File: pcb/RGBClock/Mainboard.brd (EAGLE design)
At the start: 100 x 80 mm, 88 parts, among them IC1 MCP23017SO, K1 G6K-2F, K2 G6K-2F, K3 G6K-2F, K4 G6K-2F, U1 71918-126LF, U10 2N7002-7-F, U11 2N7002-7-F, U12 2N7002-7-F, U13 NX3L1G384GW, U14 NX3L1G384GW, U15 NX3L1G384GW, U16 NX3L1G384GW, U2 LM2675M-5.0, U3 TXS0102DCUR, U4 P82B96DR, U5 TPS71533DCKR, U6 DS1338Z-33+, U7 MAX6369KA+T, U8 DRV612PW, U9 2N7002-7-F, X12 1503_09, X13 1503_09, X2 5566-4, X3 5566-8

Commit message: Mainboard + displayboard
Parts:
- removed U$1: SRR1240-680M, Bourns_By_element14_Batch_1:SRR1240
- removed U$2: 68u, MyComponents:594D-B
- removed U$3: SI4735-D50, SiliconLabs:SSOP24
- removed U$4, U$7: CDSOD323-T03C, MyComponents:SOD323
- removed U$5, U$6: SMA6F, MyComponents:DO-221AC
- removed X12: 1503_09, con-lumberg:1503_09
- added C18: 1u, rcl:C1005
- added D10: 1N4148DO35-7, diode:DO35-7
- added D3: SMA6F, MyComponents:DO-221AC
- added D5, D6: CDSOD323-T03C, MyComponents:SOD323
- added L1: SRR1240-680M, Bourns_By_element14_Batch_1:SRR1240
- added U17: 2N7002-7-F, Diodes:SOT103P240X110-3N
- added X5: 5566-8, con-molex:5566-8
- C10: value 1u -> 22p
- C11: value 1u -> 100n
- C12: value 1u -> 22n
- C13: value 22p -> 0,47u; device rcl:C1005 -> rcl:C1206
- C14: value 22p -> 2u2
- C15: value 1n -> 2u2
- C16: value 22n -> 1u
- C17: value 100n -> 1u
- C4: value 100n -> 594D686X0010C2T; device rcl:C0805 -> MyComponents:594D-B
- C5: value 0,47u -> 1n; device rcl:C1206 -> rcl:C1005
- C6: value 2u2 -> 22p
- C7: value 2u2 -> 100n; device rcl:C1005 -> rcl:C0805
- D2: value 1N4148DO35-7 -> SMA6F; device diode:DO35-7 -> MyComponents:DO-221AC
- R10, R11, R8, R9: value (none) -> 47K; device resistor:R2012 -> resistor:0204V
- R13: value 680R -> 4K7
- R14: value 680R -> A2-1; device resistor:0204V -> resistor:R0402
- R15: value 100R -> A2-0; device resistor:0204V -> resistor:R0402
- R16: value 47K -> A1-1; device resistor:0204V -> resistor:R0402
- R17: value 47K -> A1-0; device resistor:0204V -> resistor:R0402
- R18: value 47K -> A0-1; device resistor:0204V -> resistor:R0402
- R19: value 47K -> A0-0; device resistor:0204V -> resistor:R0402
- R4: value 4K7 -> 680R
- R5: value 100R -> 680R
- R6, R7: value (none) -> 100R; device resistor:R2012 -> resistor:0204V
- U10, U11, U12, U9: value 2N7002-7-F -> NX3L1G384GW; device Diodes:SOT103P240X110-3N -> NXP_By_element14_Batch_1:SOT65P212X110-5N
- U13: value NX3L1G384GW -> DRV612PW; device NXP_By_element14_Batch_1:SOT65P212X110-5N -> Texas:SOP65P640X120-14N
- U14, U15, U16: value NX3L1G384GW -> 2N7002-7-F; device NXP_By_element14_Batch_1:SOT65P212X110-5N -> Diodes:SOT103P240X110-3N
- U2: value LM2675M-5.0 -> MAX6369KA+T; device Texas:SOIC127P620X175-8N -> Maxim_By_element14_Batch_1:SOT65P280X145-8N
- U5: value TPS71533DCKR -> LM2675M-5.0; device Texas:SOT65P210X110-5N -> Texas:SOIC127P620X175-8N
- U7: value MAX6369KA+T -> SI4735-D50; device Maxim_By_element14_Batch_1:SOT65P280X145-8N -> SiliconLabs:SSOP24
- U8: value DRV612PW -> TPS71533DCKR; device Texas:SOP65P640X120-14N -> Texas:SOT65P210X110-5N
- X3: value 5566-8 -> 1503_09; device con-molex:5566-8 -> con-lumberg:1503_09
- moved X3 103.4 mm to (1.27, 59.7)
- moved R13 62.3 mm to (76.2, 38.1)
- moved R4 62.3 mm to (15.2, 50.8)
- moved C5 47.4 mm to (45.7, 29.2)
- moved C12 44.6 mm to (39.4, 31.8), turned to 0 degrees
- moved C16 44.4 mm to (82.5, 41.9)
- moved R14 44.3 mm to (40.9, 17.8), turned to 0 degrees
- moved R9 40.9 mm to (63.5, 48.3)
- moved U5 40.9 mm to (31.8, 62.2)
- moved C13 40.3 mm to (62.2, 73.7)
- moved D2 40.2 mm to (26.2, 37.8)
- moved C10 40.1 mm to (43.2, 34.3)
- moved R17 39.0 mm to (37.6, 19.1)
- moved R10 38.1 mm to (57.1, 48.3)
- moved R15 35.7 mm to (37.6, 17.8), turned to 0 degrees
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- renumbered Q3 to Q1, Q4 to Q2, X13 to X4, X7 to X1
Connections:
- net +3V3: now also C11.1, C12.1, C13.1, C17.2, R10.1, R14.2, R16.2, R18.2, R8.1, U10.5, U11.5, U12.5, U13.10, U2.4, U2.5, U2.6, U2.8, U7.20, U7.21, U8.5, U9.5; no longer C12.2, C16.1, C17.1, C5.1, R16.1, R18.1, R6.2, R8.2, R9.2, U$3.20, U$3.21, U13.5, U14.5, U15.5, U16.5, U5.5, U7.4, U7.5, U7.6, U7.8, U8.10
- net +5V: now also C4.P$1, C7.1, L1.1, U8.4; no longer C4.1, U$1.1, U$2.P$1, U2.4
- net GND: now also C10.1, C11.2, C13.2, C17.1, C18.1, C4.P$2, C6.1, C7.2, D2.AN, D3.AN, D5.P$1, D6.P$1, R11.2, R15.1, R17.1, R19.1, R9.2, U10.3, U11.3, U12.3, U13.11, U14.2, U15.2, U16.2, U17.2, U2.2, U5.6, U7.13, U7.14, U8.2, U9.3, X3.1; no longer C11.1, C12.1, C13.1, C14.1, C17.2, C4.2, C5.2, R10.1, R11.1, R17.2, R19.2, R7.1, U$2.P$2, U$3.13, U$3.14, U$4.P$1, U$5.AN, U$6.AN, U$7.P$1, U10.2, U11.2, U12.2, U14.3, U15.3, U16.3, U2.6, U5.2, U7.2, U8.11, U8.3, U9.2, X12.1
- net N$10: now also U5.1; no longer U2.1
- net N$11: now also L1.2, U5.8; no longer U$1.2, U2.8
- net N$12: now also K4.4, X5.7; no longer K3.4, X3.7
- net N$13: now also K4.3, X5.8; no longer K3.3, X3.8
- net N$18: now also U14.1; no longer U9.1
- net N$19: now also U15.1; no longer U10.1
- net N$2: now also U12.4; no longer U16.4
- net N$20: now also K1.3, X5.2; no longer K4.3, X3.2
- net N$21: now also U16.1; no longer U11.1
- net N$22: now also K1.8, U14.3; no longer K4.8, U9.3
- net N$23: now also K2.8, U15.3; no longer K1.8, U10.3
- net N$24: now also K3.8, U16.3; no longer K2.8, U11.3
- net N$25: now also C6.2, U7.3; no longer C13.2, U$3.3
- net N$26: now also C10.2, U7.19; no longer C14.2, U$3.19
- net N$27: now also U7.24, U9.1; no longer U$3.24, U13.1
- net N$28: now also U10.1, U7.23; no longer U$3.23, U14.1
- net N$29: now also C14.1, U11.2, U9.2; no longer C7.1, U13.2, U15.2
- net N$30: now also C15.2, U10.2, U12.2; no longer C9.2, U14.2, U16.2
- net N$31: now also U9.4; no longer U13.4
- net N$32: now also U10.4; no longer U14.4
- net N$33: now also U2.1; no longer U7.1
- net N$34: now also U11.4; no longer U15.4
- net N$35: now also U7.15; no longer U$3.15
- net N$36: now also C9.2, D6.P$2, R10.2, R11.1, U12.1; no longer C6.2, R18.2, R19.1, U$4.P$2, U16.1
- net N$37: now also D5.P$2, R8.2, R9.1, U11.1; no longer R16.2, R17.1, U$7.P$2, U15.1
- net N$38: now also U13.4; no longer U8.4
- net N$4: now also U7.18; no longer U$3.18
- net N$40: now also U13.2; no longer U8.2
- net N$41: now also R18.1, R19.2; no longer R6.1, R7.2
- net N$42: now also R16.1, R17.2; no longer R10.2, R8.1
- net N$43: now also R14.1, R15.2; no longer R11.2, R9.1
- net N$44: now also U13.13; no longer U8.13
- net N$45: now also R13.2; no longer R4.2
- net N$46: now also R13.1, U13.12; no longer R4.1, U8.12
- net N$47: now also R6.2, X3.2; no longer R5.2, X12.2
- net N$48: now also R6.1; no longer R5.1
- net N$49: now also R7.2, X3.3; no longer R15.2, X12.3
- net N$5: now also K1.4, X5.1; no longer K4.4, X3.1
- net N$50: now also C9.1, R7.1; no longer C6.1, R15.1
- net N$51: now also U2.7; no longer U7.7
- net N$52: now also K2.4, X5.3; no longer K1.4, X3.3
- net N$53: now also C14.2, U13.1; no longer C7.2, U8.1
- net N$54: now also C16.2, U13.9; no longer C10.2, U8.9
- net N$55: now also C15.1, U13.14; no longer C9.1, U8.14
- net N$56: now also C16.1, U13.6; no longer C10.1, U8.6
- net N$57: now also C18.2, U13.5; no longer C11.2, U8.5
- net N$58: now also C5.1; no longer C15.1
- net N$59: now also C5.2, U7.8; no longer C15.2, U$3.8
- net N$60: now also K2.3, X5.4; no longer K1.3, X3.4
- net N$61: now also C12.2, U7.22; no longer C16.2, U$3.22
- net N$62: now also U7.17; no longer U$3.17
- net N$63: now also K3.4, X5.5; no longer K2.4, X3.5
- net N$64: now also K3.3, X5.6; no longer K2.3, X3.6
- net N$7: now also U17.1; no longer U12.1
- net N$9: now also D10.A, K4.8, U17.3; no longer D2.A, K3.8, U12.3
- net SCL_LONG: now also D2.KAT, R4.1; no longer R13.1, U$5.KAT
- net SDA_LONG: now also D3.KAT, R5.1; no longer R14.1, U$6.KAT
- net VCC: now also D10.C, R4.2, R5.2, U5.7; no longer D2.C, R13.2, R14.2, U2.7
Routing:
- removed copper zone on layer 1, net GND
- removed copper zone on layer 16, net GND

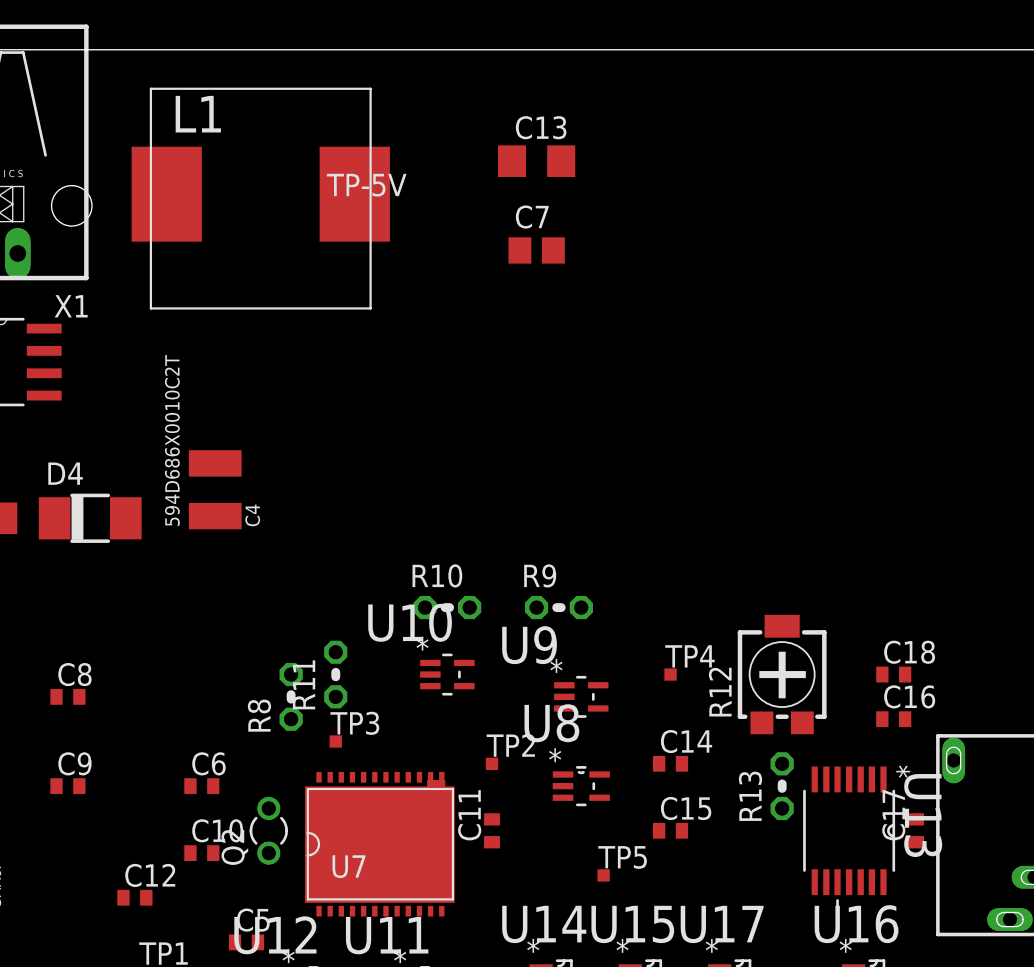
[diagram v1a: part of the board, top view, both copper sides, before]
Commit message: updating displayboard
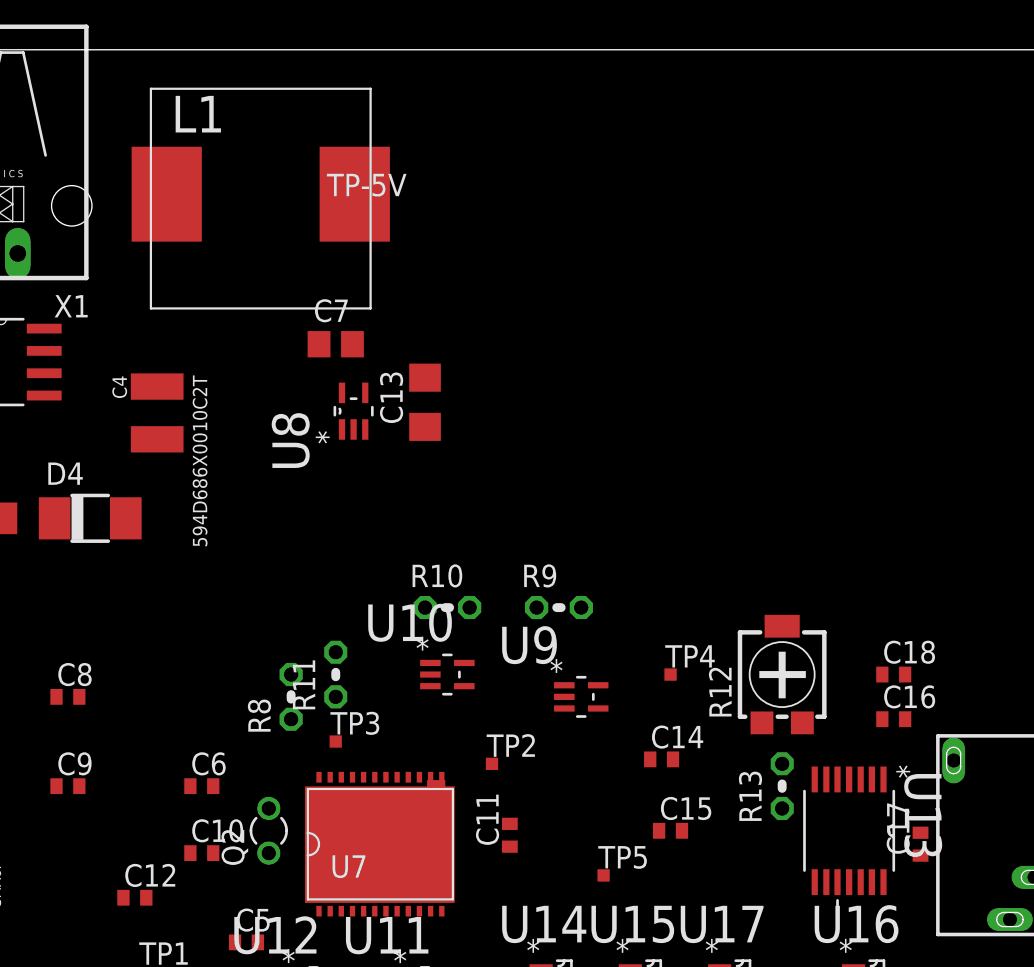
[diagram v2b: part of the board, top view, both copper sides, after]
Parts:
- moved U8 25.0 mm to (51.8, 59.4), turned to 90 degrees
- moved C13 15.1 mm to (55.9, 59.9), turned to 90 degrees
- moved C7 12.6 mm to (50.8, 63.2)
- moved C4 5.64 mm to (40.6, 59.4), turned to 180 degrees
- moved C11 1.05 mm to (60.7, 35.3)
- moved C17 0.80 mm to (84.1, 34.8)
- moved C14 0.57 mm to (69.3, 39.6)

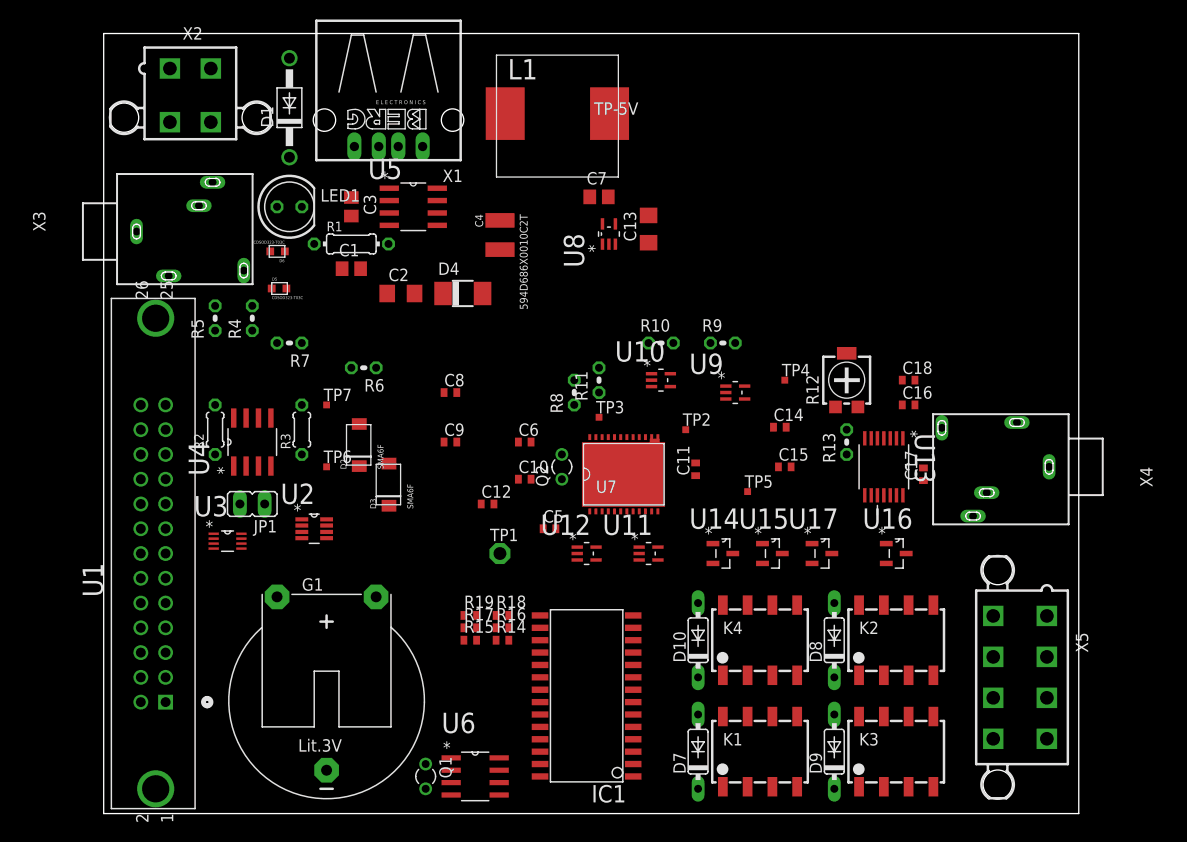
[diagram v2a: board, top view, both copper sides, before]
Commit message: 
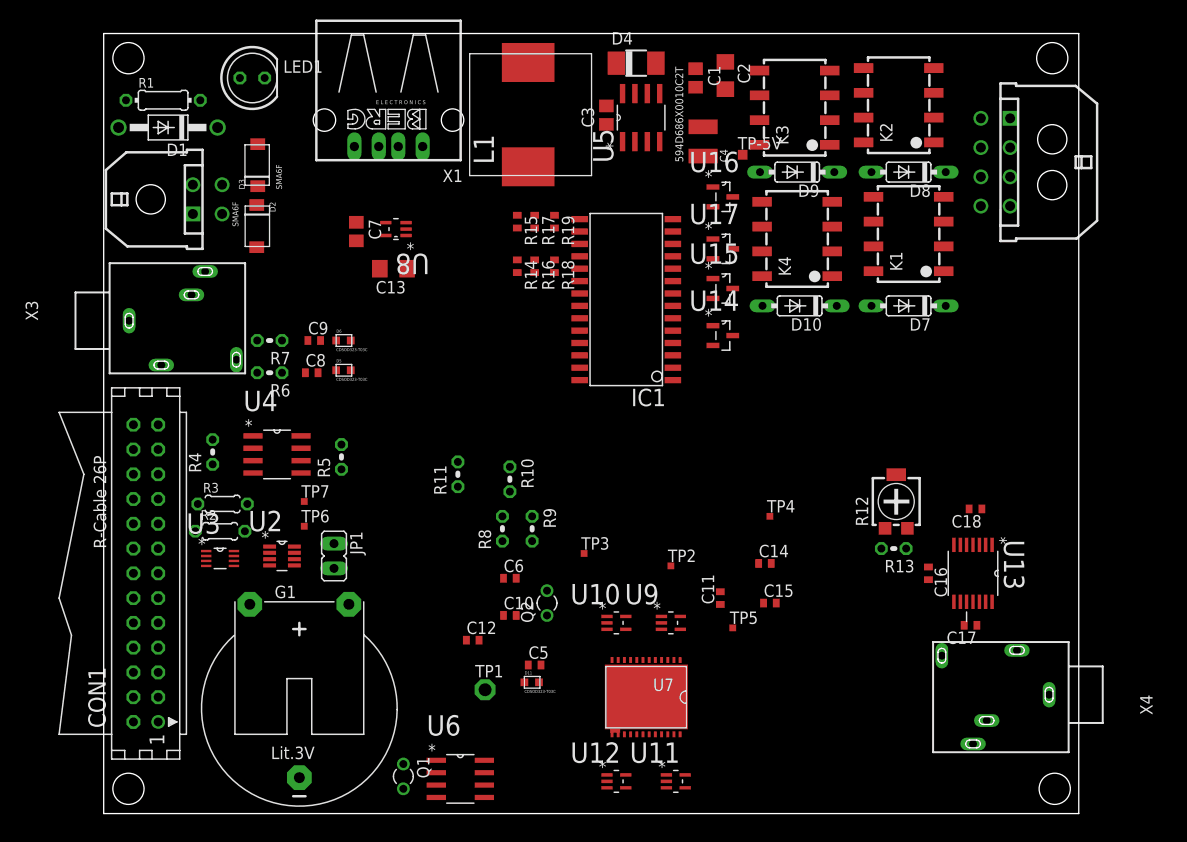
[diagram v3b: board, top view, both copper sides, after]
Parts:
- removed U1: 71918-126LF, Fci:FCI_71918-126LF
- removed X2: 5566-4, con-molex:5566-4
- added CON1: (no value), con-harting:CON26
- added D11: CDSOD323-T03C, MyComponents:SOD323
- added X6: (no value), con-molex-micro-fit-3_0:43045-0800
- X5: value 5566-8 -> (none); device con-molex:5566-8 -> con-molex-micro-fit-3_0:43045-0400
- moved X5 101.7 mm to (4.83, 63.0), turned to 270 degrees
- moved K3 66.9 mm to (70.9, 72.4), turned to 90 degrees
- moved D9 59.6 mm to (71.1, 65.8), turned to 180 degrees
- moved K1 55.2 mm to (82.5, 59.4), turned to 90 degrees
- moved K2 54.9 mm to (81.5, 72.6), turned to 90 degrees
- moved D7 50.6 mm to (82.5, 52.1), turned to 180 degrees
- moved D8 48.6 mm to (82.5, 65.8), turned to 180 degrees
- moved R15 43.2 mm to (42.4, 60.7), turned to 270 degrees
- moved R17 42.2 mm to (44.2, 60.7), turned to 270 degrees
- moved K4 41.3 mm to (71.1, 58.9), turned to 90 degrees
- moved R19 41.3 mm to (46.2, 60.7), turned to 270 degrees
- moved IC1 40.8 mm to (53.6, 52.1)
- moved U16 40.7 mm to (63.5, 63.2)
- moved C1 40.4 mm to (60.7, 75.4), turned to 270 degrees
- moved C2 40.1 mm to (63.8, 75.7), turned to 270 degrees
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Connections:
- removed net N$2: IC1.4, U12.4
- removed net N$32: IC1.2, U10.4
- removed net N$34: IC1.3, U11.4
- new net N$14: R2.1, U3.8, U4.1
- new net N$65: R3.1, U3.1, U4.7
- new net N$66: IC1.2, U10.4, U9.4
- net +3V3: now also U7.16
- net GND: now also CON1.6, D11.P$1, U7.9, X5.P$1; no longer U1.6, X2.1
- net N$1: now also X5.P$2; no longer X2.2
- net N$12: now also X6.P$7; no longer X5.7
- net N$13: now also X6.P$8; no longer X5.8
- net N$20: now also X6.P$2; no longer X5.2
- net N$3: now also CON1.3; no longer U1.3
- net N$31: now also IC1.3, U11.4, U12.4; no longer IC1.1, U9.4
- net N$33: now also IC1.5; no longer IC1.7
- net N$35: now also IC1.4; no longer IC1.5
- net N$38: now also IC1.1; no longer IC1.6
- net N$4: no longer R3.1, U3.8, U4.7
- net N$5: now also X6.P$1; no longer X5.1
- net N$52: now also X6.P$3; no longer X5.3
- net N$59: now also D11.P$2
- net N$6: now also CON1.5; no longer U1.5
- net N$60: now also X6.P$4; no longer X5.4
- net N$62: no longer R2.1, U3.1, U4.1
- net N$63: now also X6.P$5; no longer X5.5
- net N$64: now also X6.P$6; no longer X5.6
- net N$8: now also CON1.1; no longer U1.1
- net SCL_LONG: now also D3.KAT, R5.1, U4.5, U4.6, X5.P$4; no longer D2.KAT, R4.1, U4.2, U4.3, X2.3
- net SDA_LONG: now also D2.KAT, R4.1, U4.2, U4.3, X5.P$3; no longer D3.KAT, R5.1, U4.5, U4.6, X2.4

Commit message: 
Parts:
- D4: value (none) -> B130-13-F
- Q1, Q2: value (none) -> 32.768KHz
- R12: value (none) -> 100k
- R2, R3: value (none) -> 3k3
- X5: value (none) -> 43045-0400
- X6: value (none) -> 43045-0800
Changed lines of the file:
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@@
 <attribute name="OC_FARNELL" value="1713823" x="160.02" y="-17.018" size="1.778" layer="27" display="off"/>
 </element>
-<element name="R3" library="resistor" package="0204/5" value="" x="12.192" y="31.75"/>
-<element name="R2" library="resistor" package="0204/5" value="" x="11.938" y="28.956"/>
+<element name="R3" library="resistor" package="0204/5" value="3k3" x="12.192" y="31.75"/>
+<element name="R2" library="resistor" package="0204/5" value="3k3" x="11.938" y="28.956"/>
 <element name="U8" library="Texas" package="SOT65P210X110-5N" value="TPS71533DCKR" x="29.972" y="59.944" rot="R180">
 <attribute name="PACKAGE" value="SC-70-5" x="-3.048" y="125.984" size="1.778" layer="27" rot="R180" display="off"/>
@@
 <element name="C2" library="rcl" package="C1206" value="4,7u" x="63.754" y="75.692" rot="R270"/>
 <element name="C1" library="rcl" package="C0805" value="100n" x="60.706" y="75.438" rot="R270"/>
-<element name="D4" library="diode" package="DO-214AC" value="" x="54.61" y="76.962"/>
+<element name="D4" library="diode" package="DO-214AC" value="B130-13-F" x="54.61" y="76.962"/>
 <element name="C7" library="rcl" package="C0805" value="100n" x="25.908" y="59.69" rot="R270"/>
 <element name="C13" library="rcl" package="C1206" value="0,47u" x="29.718" y="55.88" rot="R180"/>
@@
 <element name="R17" library="resistor" package="R0402" value="A1-0" x="44.196" y="60.706" rot="R270"/>
 <element name="R15" library="resistor" package="R0402" value="A2-0" x="42.418" y="60.706" rot="R270"/>
-<element name="R12" library="resistor" package="RTRIM4G/J" value="" x="81.28" y="32.004"/>
+<element name="R12" library="resistor" package="RTRIM4G/J" value="100k" x="81.28" y="32.004"/>
 <element name="R4" library="resistor" package="0204V" value="680R" x="11.176" y="37.084" rot="R90"/>
 <element name="R5" library="resistor" package="0204V" value="680R" x="24.384" y="36.576" rot="R90"/>
@@
 <element name="C18" library="rcl" package="C1005" value="1u" x="89.408" y="31.242" rot="R180"/>
 <element name="C17" library="rcl" package="C1005" value="1u" x="88.9" y="19.304" rot="R180"/>
-<element name="Q1" library="crystal" package="TC26V" value="" x="30.734" y="3.81" rot="R270">
+<element name="Q1" library="crystal" package="TC26V" value="32.768KHz" x="30.734" y="3.81" rot="R270">
 <attribute name="OC_NEWARK" value="unknown" x="-79.756" y="-106.68" size="1.778" layer="27" rot="R270" display="off"/>
 <attribute name="MPN" value="" x="-79.756" y="-106.68" size="1.778" layer="27" rot="R270" display="off"/>
@@
 <attribute name="OC_FARNELL" value="unknown" x="-79.756" y="-106.68" size="1.778" layer="27" rot="R270" display="off"/>
 </element>
-<element name="Q2" library="crystal" package="TC26V" value="" x="45.466" y="21.59" rot="R90">
+<element name="Q2" library="crystal" package="TC26V" value="32.768KHz" x="45.466" y="21.59" rot="R90">
 <attribute name="OC_NEWARK" value="unknown" x="162.306" y="36.83" size="1.778" layer="27" rot="R90" display="off"/>
 <attribute name="MPN" value="" x="162.306" y="36.83" size="1.778" layer="27" rot="R90" display="off"/>
@@
 <element name="C4" library="MyComponents" package="594D-B" value="594D686X0010C2T" x="61.468" y="68.834"/>
 <element name="L1" library="Bourns_By_element14_Batch_1" package="SRR1240" value="SRR1240-680M" x="43.434" y="71.628" rot="R90"/>
-<element name="X6" library="con-molex-micro-fit-3_0" package="43045-0800" value="" x="97.282" y="66.802" rot="R90"/>
+<element name="X6" library="con-molex-micro-fit-3_0" package="43045-0800" value="43045-0800" x="97.282" y="66.802" rot="R90"/>
 <element name="D11" library="MyComponents" package="SOD323" value="CDSOD323-T03C" x="43.942" y="13.462"/>
-<element name="X5" library="con-molex-micro-fit-3_0" package="43045-0400" value="" x="4.826" y="62.992" rot="R270">
+<element name="X5" library="con-molex-micro-fit-3_0" package="43045-0400" value="43045-0400" x="4.826" y="62.992" rot="R270">
 <attribute name="MATERIAL" value="" x="4.826" y="62.992" size="1.778" layer="27" rot="R270" display="off"/>
 </element>
